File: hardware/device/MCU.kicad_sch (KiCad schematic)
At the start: 26 parts, among them SW24 NRST, SW25 BOOT0, U1 BMDU, U18 STM32H743ZIT6

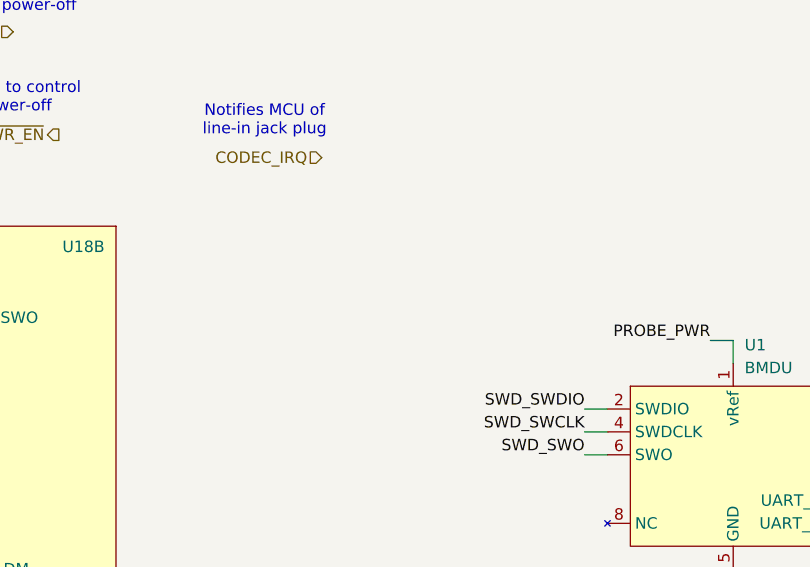
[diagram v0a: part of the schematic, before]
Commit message: feat: keypad schematic cleanup
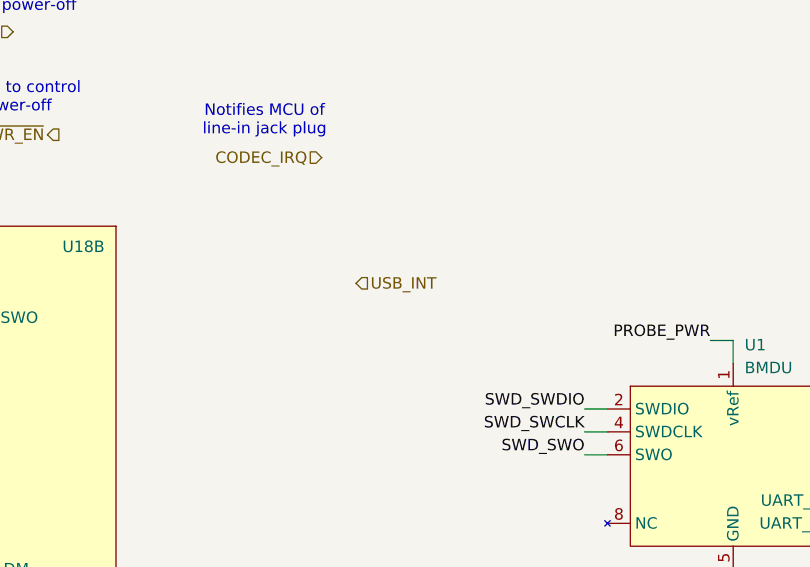
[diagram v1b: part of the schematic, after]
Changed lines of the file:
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@@
+		)
+	)
+	(hierarchical_label "USB_INT"
+		(shape input)
+		(at 118.11 154.94 0)
+		(effects
+			(font
+				(size 1.27 1.27)
+				(thickness 0.1588)
+			)
+			(justify left)
 		)
 	)

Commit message: chore: schematic organization
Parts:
- added R36, R37: 4.7k, Resistor_SMD:R_0402_1005Metric, symbol Device:R
- C87: footprint Capacitor_SMD:C_0201_0603Metric -> Capacitor_SMD:C_0402_1005Metric
- R22, R64: footprint Resistor_SMD:R_0201_0603Metric_Pad0.64x0.40mm_HandSolder -> Resistor_SMD:R_0402_1005Metric
- U18: JLC (none) -> C114408
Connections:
- net +3.3V: now also U18.95 (VDD33_USB), R36.1, R37.1
- net I2C.SCL: now also R37.2
- net I2C.SDA: now also R36.2
- net USB_VBUS: now reaches U18.74 (PB13)
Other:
- note removed: "PWR_FLAG is required for the ERC to properly see this filtering as a VDDA "source""
- note removed: "TODO: I2C Pullups"
- moved on the sheet: C88, C89, C90, FB9

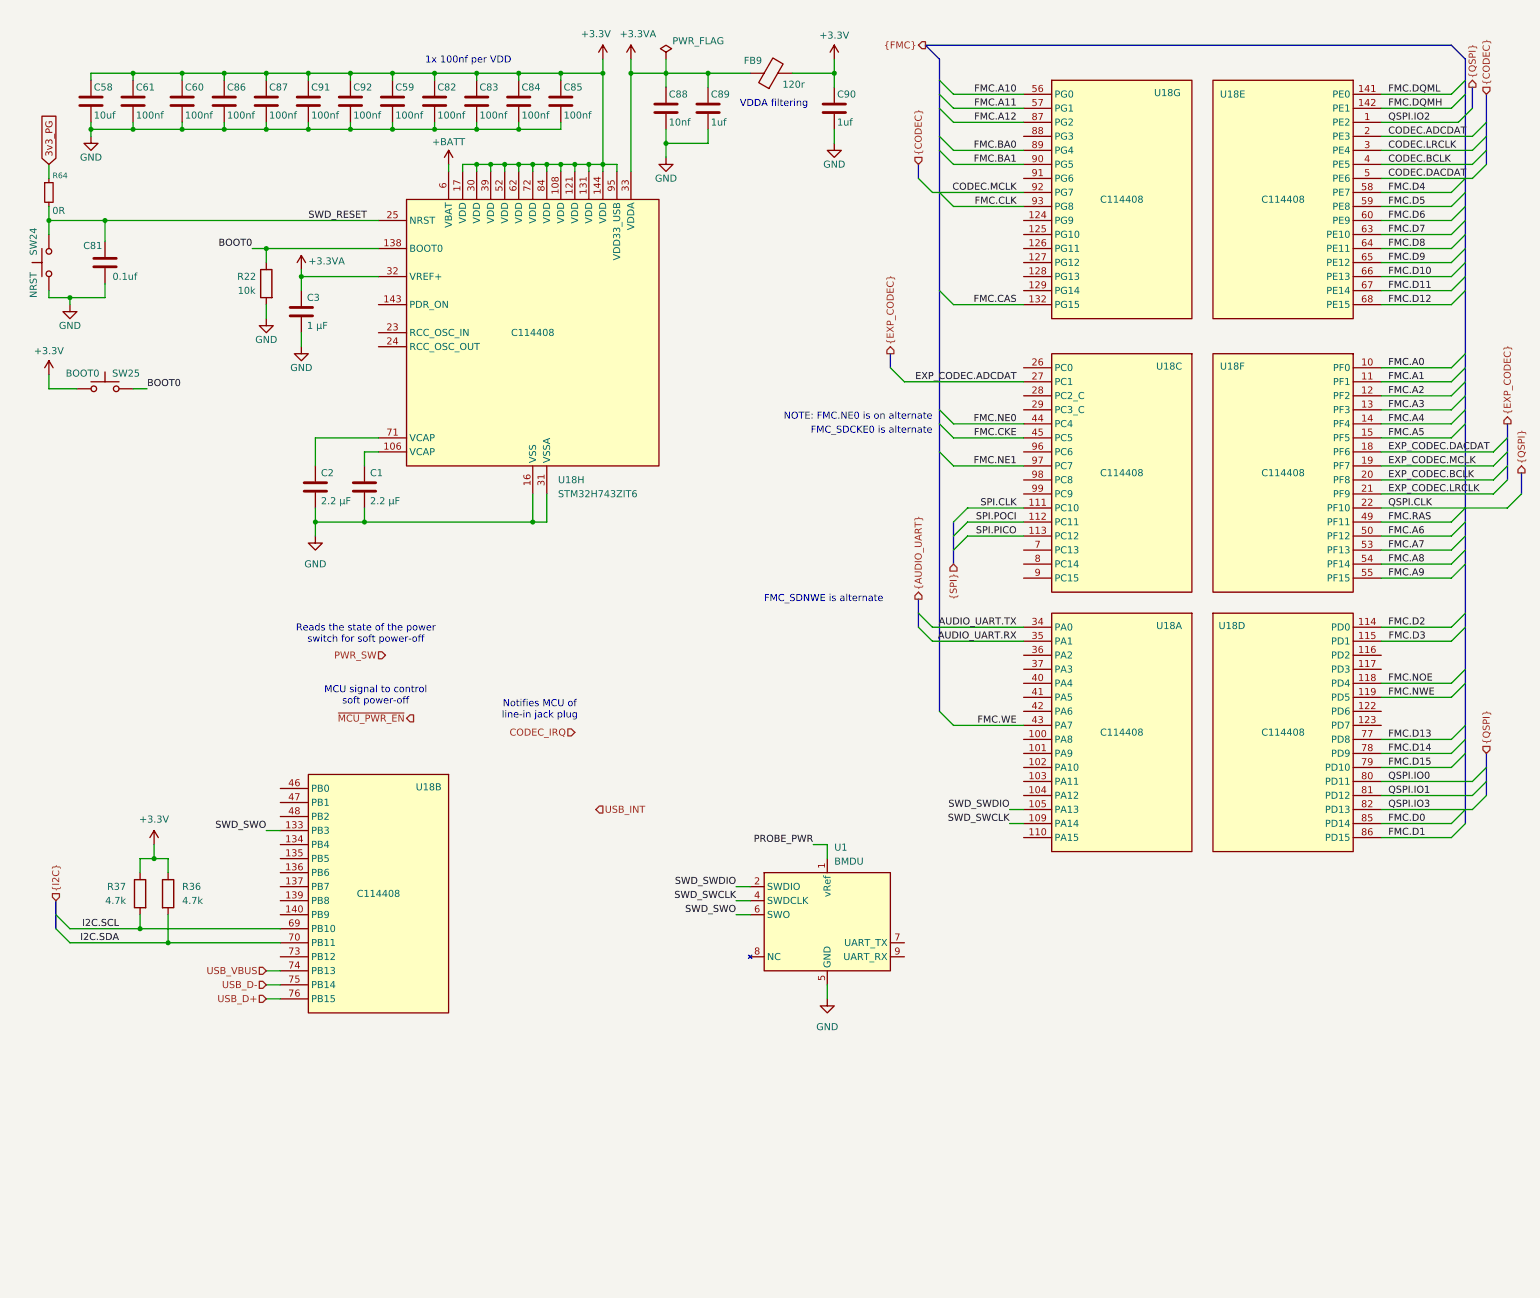
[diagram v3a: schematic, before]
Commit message: fix: add reset MCU alternate function labels
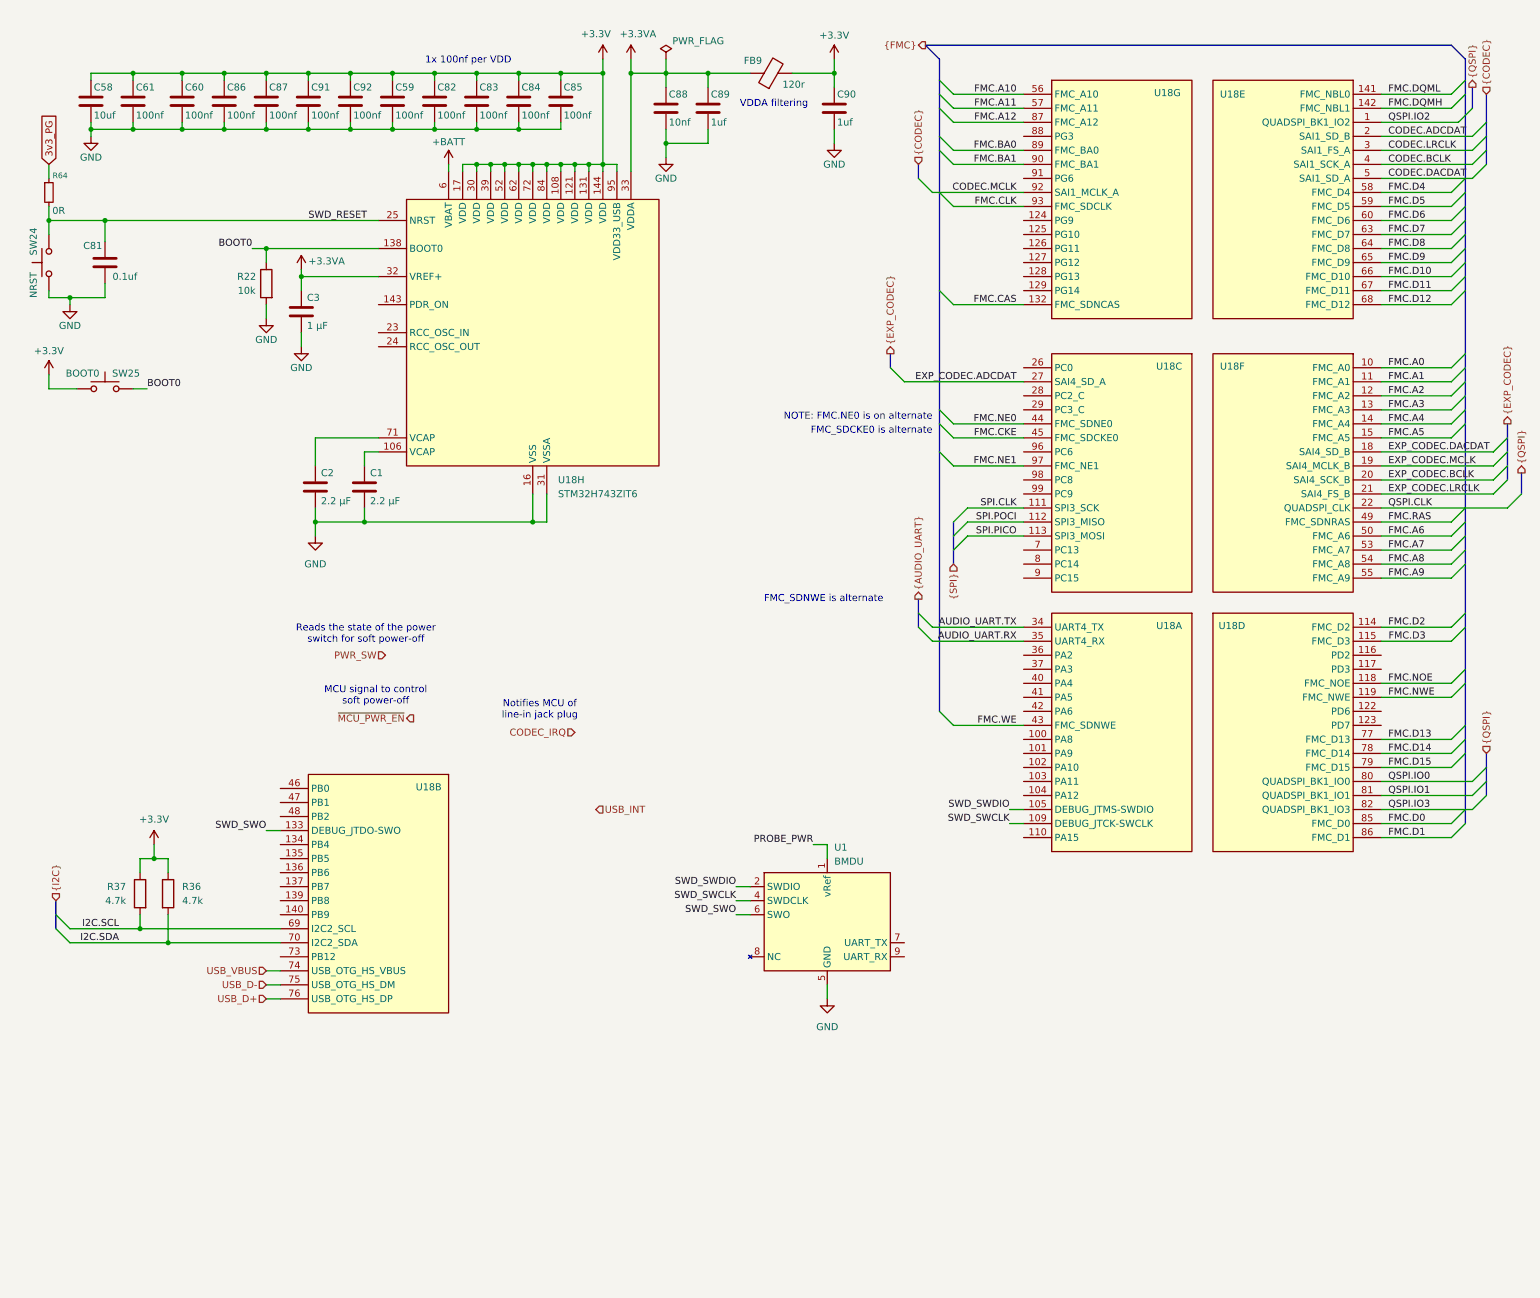
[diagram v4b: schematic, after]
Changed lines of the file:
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@@
 					(size 1.27 1.27)
 				)
+				(hide yes)
 			)
 		)
@@
 					(size 1.27 1.27)
 				)
+				(hide yes)
 			)
 		)
@@
 		)
 		(pin "34"
+			(alternate "UART4_TX")
 		)
 		(pin "35"
+			(alternate "UART4_RX")
 		)
 		(pin "36"
@@
 		)
 		(pin "43"
+			(alternate "FMC_SDNWE")
 		)
 		(pin "100"
@@
 		)
 		(pin "105"
+			(alternate "DEBUG_JTMS-SWDIO")
 		)
 		(pin "109"
+			(alternate "DEBUG_JTCK-SWCLK")
 		)
 		(pin "69"
@@
 					(size 1.27 1.27)
 				)
+				(hide yes)
 			)
 		)
@@
 		)
 		(pin "114"
+			(alternate "FMC_D2")
 		)
 		(pin "115"
+			(alternate "FMC_D3")
 		)
 		(pin "116"
@@
 		)
 		(pin "118"
+			(alternate "FMC_NOE")
 		)
 		(pin "119"
+			(alternate "FMC_NWE")
 		)
 		(pin "122"
@@
 		)
 		(pin "77"
+			(alternate "FMC_D13")
 		)
 		(pin "78"
+			(alternate "FMC_D14")
 		)
 		(pin "79"
+			(alternate "FMC_D15")
 		)
 		(pin "80"
+			(alternate "QUADSPI_BK1_IO0")
 		)
 		(pin "81"
+			(alternate "QUADSPI_BK1_IO1")
 		)
 		(pin "82"
+			(alternate "QUADSPI_BK1_IO3")
 		)
 		(pin "85"
+			(alternate "FMC_D0")
 		)
 		(pin "86"
+			(alternate "FMC_D1")
 		)
 		(pin "94"
@@
 					(size 1.27 1.27)
 				)
+				(hide yes)
 			)
 		)
 		(pin "142"
+			(alternate "FMC_NBL1")
 		)
 		(pin "23"
@@
 		)
 		(pin "63"
+			(alternate "FMC_D7")
 		)
 		(pin "6"
 		)
 		(pin "2"
+			(alternate "SAI1_SD_B")
 		)
 		(pin "106"
 		)
 		(pin "65"
+			(alternate "FMC_D9")
 		)
 		(pin "17"
 		)
 		(pin "141"
+			(alternate "FMC_NBL0")
 		)
 		(pin "60"
+			(alternate "FMC_D6")
 		)
 		(pin "67"
+			(alternate "FMC_D11")
 		)
 		(pin "68"
+			(alternate "FMC_D12")
 		)
 		(pin "90"
@@
 		)
 		(pin "64"
+			(alternate "FMC_D8")
 		)
 		(pin "20"
@@
 		)
 		(pin "3"
+			(alternate "SAI1_FS_A")
 		)
 		(pin "138"
 		)
 		(pin "59"
+			(alternate "FMC_D5")
 		)
 		(pin "87"
@@
 		)
 		(pin "1"
+			(alternate "QUADSPI_BK1_IO2")
 		)
 		(pin "71"
@@
 		)
 		(pin "4"
+			(alternate "SAI1_SCK_A")
 		)
 		(pin "14"
@@
 		)
 		(pin "5"
+			(alternate "SAI1_SD_A")
 		)
 		(pin "58"
+			(alternate "FMC_D4")
 		)
 		(pin "49"
@@
 		)
 		(pin "66"
+			(alternate "FMC_D10")
 		)
 		(pin "143"
@@
 					(size 1.27 1.27)
 				)
+				(hide yes)
 			)
 		)
@@
 		)
 		(pin "22"
+			(alternate "QUADSPI_CLK")
 		)
 		(pin "63"
@@
 		)
 		(pin "18"
+			(alternate "SAI4_SD_B")
 		)
 		(pin "15"
+			(alternate "FMC_A5")
 		)
 		(pin "11"
+			(alternate "FMC_A1")
 		)
 		(pin "64"
 		)
 		(pin "20"
+			(alternate "SAI4_SCK_B")
 		)
 		(pin "19"
+			(alternate "SAI4_MCLK_B")
 		)
 		(pin "12"
+			(alternate "FMC_A2")
 		)
 		(pin "21"
+			(alternate "SAI4_FS_B")
 		)
 		(pin "3"
@@
 		)
 		(pin "10"
+			(alternate "FMC_A0")
 		)
 		(pin "4"
 		)
 		(pin "14"
+			(alternate "FMC_A4")
 		)
 		(pin "13"
+			(alternate "FMC_A3")
 		)
 		(pin "129"
 		)
 		(pin "50"
+			(alternate "FMC_A6")
 		)
 		(pin "5"
@@
 		)
 		(pin "49"
+			(alternate "FMC_SDNRAS")
 		)
 		(pin "30"
@@
 		)
 		(pin "54"
+			(alternate "FMC_A8")
 		)
 		(pin "53"
+			(alternate "FMC_A7")
 		)
 		(pin "125"
@@
 		)
 		(pin "55"
+			(alternate "FMC_A9")
 		)
 		(pin "56"
@@
 					(size 1.27 1.27)
 				)
+				(hide yes)
 			)
 		)
@@
 		)
 		(pin "44"
+			(alternate "FMC_SDNE0")
 		)
 		(pin "45"
+			(alternate "FMC_SDCKE0")
 		)
 		(pin "51"
@@
 		)
 		(pin "111"
+			(alternate "SPI3_SCK")
 		)
 		(pin "112"
+			(alternate "SPI3_MISO")
 		)
 		(pin "113"
+			(alternate "SPI3_MOSI")
 		)
 		(pin "7"
@@
 		)
 		(pin "97"
+			(alternate "FMC_NE1")
 		)
 		(pin "98"
@@
 		)
 		(pin "27"
+			(alternate "SAI4_SD_A")
 		)
 		(pin "28"
@@
 					(size 1.27 1.27)
 				)
+				(hide yes)
 			)
 		)
@@
 		)
 		(pin "90"
+			(alternate "FMC_BA1")
 		)
 		(pin "18"
@@
 		)
 		(pin "87"
+			(alternate "FMC_A12")
 		)
 		(pin "127"
@@
 		)
 		(pin "132"
+			(alternate "FMC_SDNCAS")
 		)
 		(pin "10"
@@
 		)
 		(pin "56"
+			(alternate "FMC_A10")
 		)
 		(pin "57"
+			(alternate "FMC_A11")
 		)
 		(pin "92"
+			(alternate "SAI1_MCLK_A")
 		)
 		(pin "89"
+			(alternate "FMC_BA0")
 		)
 		(pin "91"
 		)
 		(pin "93"
+			(alternate "FMC_SDCLK")
 		)
 		(pin "124"
@@
 					(size 1.27 1.27)
 				)
+				(hide yes)
 			)
 		)
@@
 		)
 		(pin "133"
+			(alternate "DEBUG_JTDO-SWO")
 		)
 		(pin "134"
@@
 		)
 		(pin "76"
+			(alternate "USB_OTG_HS_DP")
 		)
 		(pin "26"
@@
 		)
 		(pin "69"
+			(alternate "I2C2_SCL")
 		)
 		(pin "70"
+			(alternate "I2C2_SDA")
 		)
 		(pin "73"
@@
 		)
 		(pin "74"
+			(alternate "USB_OTG_HS_VBUS")
 		)
 		(pin "75"
+			(alternate "USB_OTG_HS_DM")
 		)
 		(pin "55"

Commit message: feat: audio system routing
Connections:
- net CODEC_IRQ: now also U18.110 (PA15)
- net MIC_SELECT: now reaches U18.98 (PC8)
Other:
- note added: "Selects if line-in is a mic or aux input"
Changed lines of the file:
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@@
 		)
 	)
+	(text "Selects if line-in is\na mic or aux input"
+		(exclude_from_sim no)
+		(at 167.64 91.44 0)
+		(effects
+			(font
+				(size 1.27 1.27)
+				(color 132 132 132 1)
+			)
+		)
+	)
 	(text "1x 100nf per VDD"
 		(exclude_from_sim no)
@@
 	(text "Notifies MCU of\nline-in jack plug"
 		(exclude_from_sim no)
-		(at 107.95 136.906 0)
+		(at 171.45 155.956 0)
 		(effects
 			(font
@@
 	(wire
 		(pts
+			(xy 177.8 160.02) (xy 195.58 160.02)
+		)
+		(stroke
+			(width 0)
+			(type default)
+		)
+	)
+	(wire
+		(pts
 			(xy 182.88 139.7) (xy 195.58 139.7)
 		)
@@
 	(wire
 		(pts
+			(xy 173.99 95.25) (xy 195.58 95.25)
+		)
+		(stroke
+			(width 0)
+			(type default)
+		)
+	)
+	(wire
+		(pts
 			(xy 58.42 30.48) (xy 58.42 31.75)
 		)
@@
 		)
 	)
+	(hierarchical_label "MIC_SELECT"
+		(shape input)
+		(at 173.99 95.25 180)
+		(effects
+			(font
+				(size 1.27 1.27)
+			)
+			(justify right)
+		)
+	)
 	(hierarchical_label "USB_D+"
 		(shape input)
@@
 	(hierarchical_label "CODEC_IRQ"
 		(shape input)
-		(at 114.3 140.97 180)
+		(at 177.8 160.02 180)
 		(effects
 			(font
